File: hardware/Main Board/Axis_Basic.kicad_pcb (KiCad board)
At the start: 4 copper layers, 42 x 42 mm, 78 parts, among them J1 USB4105-GF-A, J2 JST_PH, J3 JST_SH, J4 S2B-PH-K-S, J5 JST_SH, J6 1-84952-4, SW1 RKB2SJK, SW2 RKB2SJK, U1 TLV493D, U2 UA78M33CDCYR, U3 ATSAMD51J19A-AUT, U4 TMC2209-LA, U5 AT25040B-MAHL-T, Y1 32.768

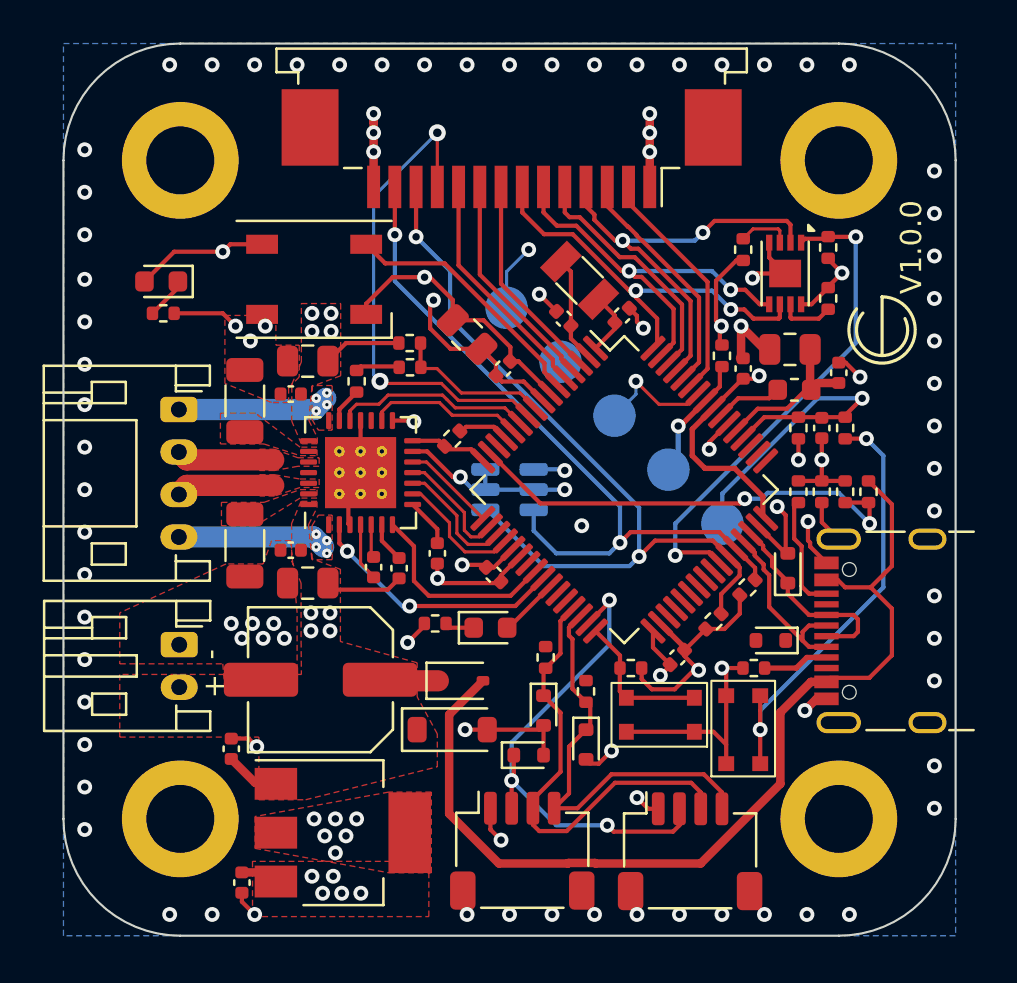
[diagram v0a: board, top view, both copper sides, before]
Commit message: Fix missed connections
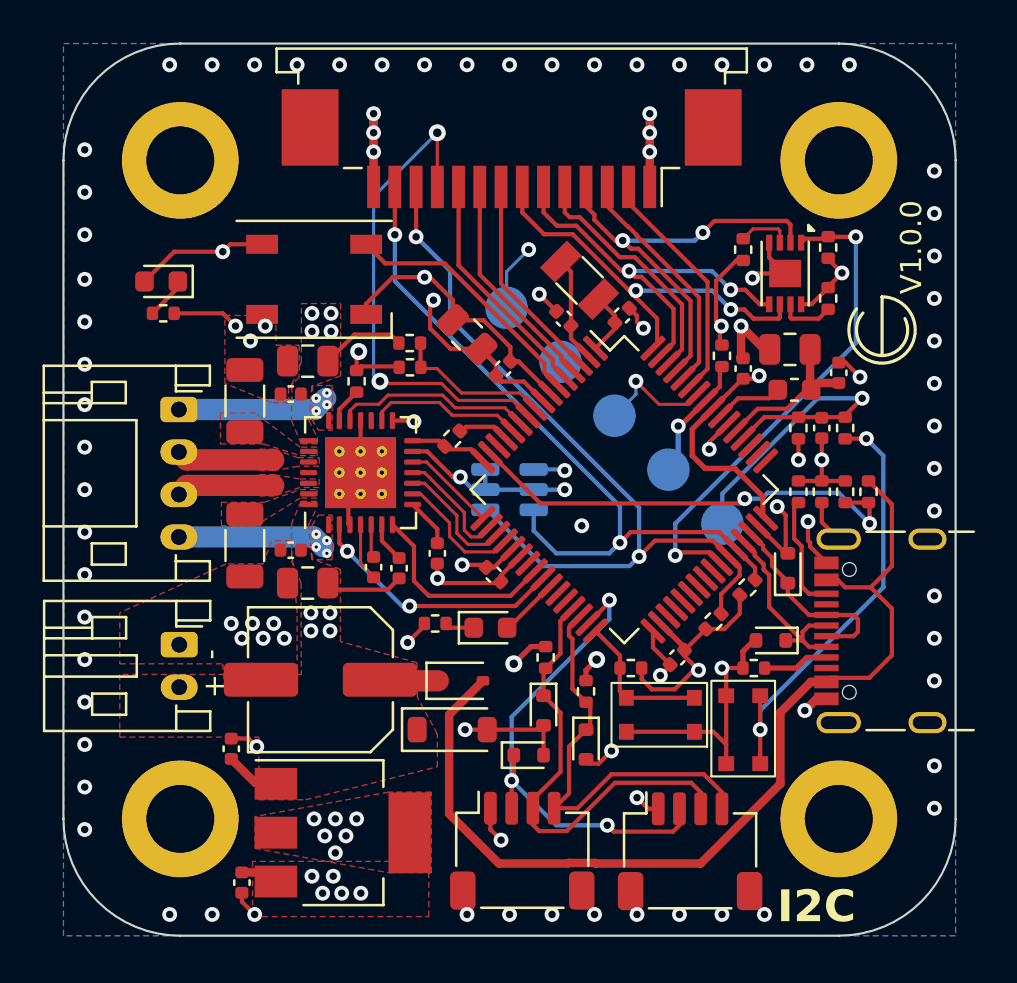
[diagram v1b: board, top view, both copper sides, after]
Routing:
- net +3.3V: track 60.8 -> 63.8 mm, vias 19 -> 21
- net GND: track 92.6 -> 95.1 mm, vias 102 -> 101
- net D-: track 8.70 -> 9.50 mm
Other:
- board text added: "I2C"

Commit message: PCB V1.1.0
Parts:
- removed the D5 at (133.6, 90.2)
- removed the R10 at (133.7, 91.7)
- removed the R11 at (161.0, 88.7)
- removed the R12 at (165.0, 91.0)
- removed the R13 at (165.0, 88.6)
- added C19: 100n, Capacitor_SMD:C_0402_1005Metric, F.Cu at (139.1, 89.3)
- added D6: XZMDK54W-1, LED_SMD:LED_0603_1608Metric, F.Cu at (166.9, 94.4)
- added R18: 1k, Resistor_SMD:R_0402_1005Metric, F.Cu at (166.9, 97.1)
- D1: value NSR0530HT1G -> PMEG3020EJ; footprint Diode_SMD:D_SOD-323 -> Diode_SMD:D_SOD-323F
- U5: value AT25040B-MAHL-T -> 24AA02E-OT; footprint Package_DFN_QFN:DFN-8-1EP_3x2mm_P0.5mm_EP1.3x1.5mm -> Package_TO_SOT_SMD:SOT-23-5
- moved U5 21.2 mm to (141.8, 89.3), turned to 180 degrees
- moved D10 6.01 mm to (134.8, 90.5)
- moved R10 2.19 mm to (159.6, 106.1)
- moved R9 2.19 mm to (161.2, 104.7)
- moved C4 0.22 mm to (137.2, 118.6)
- renumbered 3.3V to 3.3V1, C16 to C10, C19 to C11, C3 to C12, C4 to C13, C5 to C14, C6 to C15, C7 to C16, C8 to C17, C9 to C18, C18 to C2, C10 to C20, C11 to C21, C17 to C3, C2 to C4, C12 to C5, C13 to C6, C14 to C7, C20 to C8, C15 to C9, CLK to CLK1, D7 to D10, D3 to D2, D6 to D3, D8 to D5, D9 to D7, D10 to D8, D2 to D9, GND to GND1, J5 to J4, J4 to J5, R19 to R10, R18 to R11, R17 to R12, R5 to R13, R6 to R14, R7 to R15, R8 to R16, R9 to R17, R16 to R19, R14 to R20, R15 to R21, R22 to R4, R21 to R5, R4 to R6, R23 to R7, R24 to R8, R20 to R9, RST to RST1, DIO to SIO1
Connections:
- net PA03 renamed AUX4
- net PB04 renamed AUX5
- net PB07 renamed AUX6
- net PB30 renamed AUX1
- net PB31 renamed AUX2
- C3 pad 2: PA02 -> Net-(U3-PA01/S1.1)
- J2 pad 1: MOTOR_A1 -> MOTOR_A2
- J2 pad 2: MOTOR_B1 -> MOTOR_A1
- J2 pad 3: MOTOR_A2 -> MOTOR_B1
- J6 pad 8: PA02 -> AUX3
- U3 pad 2: PA02 -> Net-(U3-PA01/S1.1)
- U3 pad 3: PA02 -> AUX3
- U3 pad 42: EEPROM_CS -> unconnected-(U3-PA21/S5.3/S3.3-Pad42)
- U3 pad 43: SCL1 -> SDA1
- U3 pad 44: SDA1 -> SCL1
- U4 pad 21: MOTOR_A1 -> MOTOR_A2
- U4 pad 24: MOTOR_B1 -> MOTOR_A1
- U4 pad 26: MOTOR_A2 -> MOTOR_B1
- U5 pad 1: EEPROM_CS -> SCL1
- U5 pad 2: MISO -> GND
- U5 pad 3: Net-(U5-~{WP}) -> SDA1
- U5 pad 4: GND -> +3.3V
- U5 pad 5: MOSI -> unconnected-(U5-NC-Pad5)
- Y1 pad 2: PA02 -> Net-(U3-PA01/S1.1)
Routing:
- net EEPROM_CS: track 23.6 -> 0.00 mm, vias 2 -> 0
- net PA02: track 14.8 -> 0.00 mm
- net NEOPIX: track 12.0 -> 22.9 mm, vias 0 -> 2
- net AUX3: track 0.00 -> 9.85 mm
- net MISO: track 20.6 -> 11.0 mm, vias 2 -> 0
- net SCK: track 19.3 -> 11.5 mm, vias 2 -> 0
- net MOSI: track 18.9 -> 11.5 mm, vias 2 -> 0
- net RESET: track 16.5 -> 11.0 mm
- net AUX6: track 23.3 -> 17.9 mm
- net Net-(U3-PA01/S1.1): track 0.00 -> 4.96 mm
- net GND: track 95.1 -> 92.1 mm, vias 101 -> 92
- net Net-(U5-~{HOLD}): track 2.60 -> 0.00 mm
- net Net-(U5-~{WP}): track 2.52 -> 0.00 mm
- net MOTOR_A1: track 7.14 -> 4.62 mm, vias 4 -> 0
- net MOTOR_A2: track 4.68 -> 7.14 mm, vias 0 -> 4
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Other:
- board text added: "3.3V"
- board text added: "Aux Port"
- board text added: "CLK"
- board text added: "DIO"
- board text added: "GND"
- board text added: "Motor"
- board text added: "RST"
- board text added: "V1.1.0"
- board text removed: "V1.0.0"

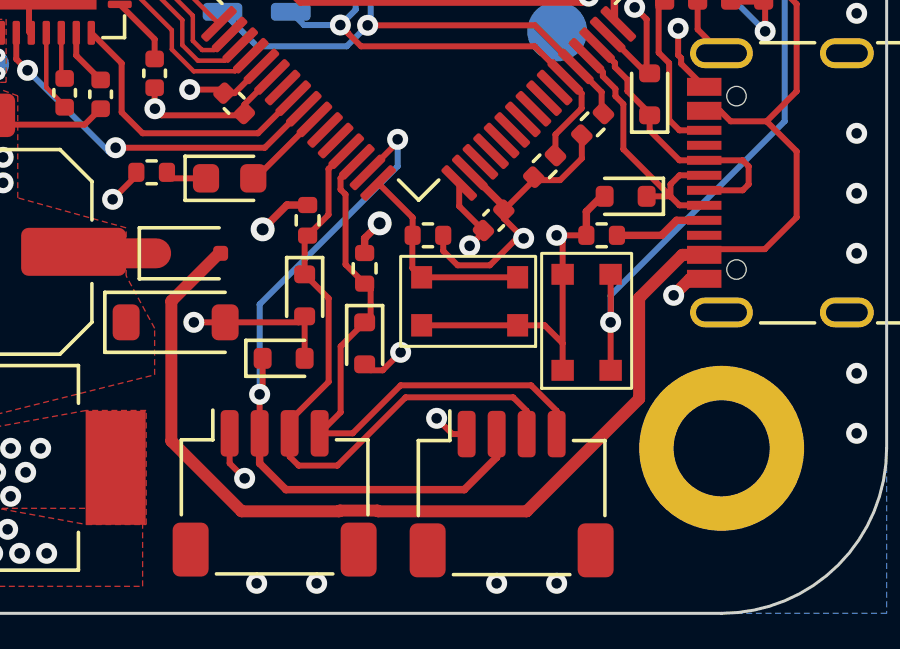
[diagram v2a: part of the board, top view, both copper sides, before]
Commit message: Fix resistor values
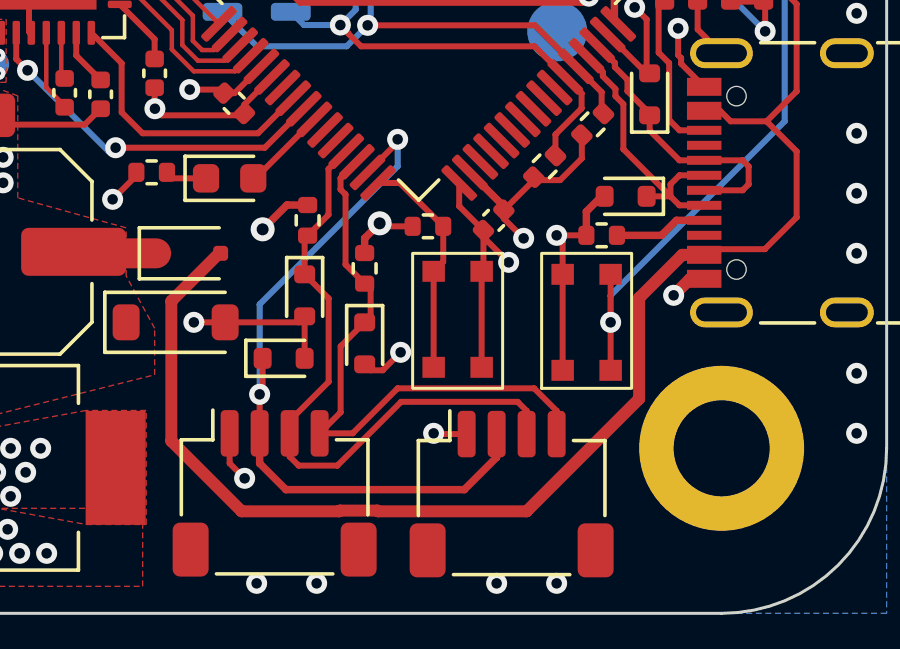
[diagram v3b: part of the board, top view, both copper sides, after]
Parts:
- moved SW2 0.72 mm to (156.7, 111.2), turned to -90 degrees
- moved R17 0.30 mm to (155.7, 108.1), turned to 0 degrees
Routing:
- net +3.3V: track 62.2 -> 59.6 mm
- net User_Input: track 6.95 -> 7.60 mm

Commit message: Update flash part number
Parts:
- C1: value 0.33u -> 1u
- D2: value MMSZ5254B -> MMSZ5254B
- R13: value 300 -> 100
- U5: value 24AA02E-OT -> AT24MAC402
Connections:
- U3 pad 26: USR_LED -> unconnected-(U3-PB13/S4.1-Pad26)
- U3 pad 28: unconnected-(U3-PB15/S4.3-Pad28) -> USR_LED
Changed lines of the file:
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@@
 	(net 64 "AUX4")
 	(net 65 "unconnected-(U3-PA19{slash}S1.3{slash}S3.3-Pad38)")
-	(net 66 "unconnected-(U3-PB15{slash}S4.3-Pad28)")
+	(net 66 "unconnected-(U3-PB13{slash}S4.1-Pad26)")
 	(net 67 "unconnected-(U3-PB17{slash}S5.1-Pad40)")
 	(net 68 "AUX3")
@@
 			)
 		)
-		(property "Value" "0.33u"
+		(property "Value" "1u"
 			(at 0 1.16 90)
 			(layer "F.Fab")
@@
 			)
 		)
-		(property "Value" "24AA02E-OT"
+		(property "Value" "AT24MAC402"
 			(at 0 2.4 0)
 			(layer "F.Fab")
@@
 			)
 		)
-		(property "Value" "300"
+		(property "Value" "100"
 			(at 0 1.17 90)
 			(layer "F.Fab")
@@
 			)
 		)
-		(property "Value" "	MMSZ5254B"
+		(property "Value" "MMSZ5254B"
 			(at 0 2.1 0)
 			(layer "F.Fab")
@@
 			(layers "F.Cu" "F.Paste" "F.Mask")
 			(roundrect_rratio 0.25)
-			(net 56 "USR_LED")
+			(net 66 "unconnected-(U3-PB13{slash}S4.1-Pad26)")
 			(pinfunction "PB13/S4.1")
 			(pintype "bidirectional")
@@
 			(layers "F.Cu" "F.Paste" "F.Mask")
 			(roundrect_rratio 0.25)
-			(net 66 "unconnected-(U3-PB15{slash}S4.3-Pad28)")
+			(net 56 "USR_LED")
 			(pinfunction "PB15/S4.3")
-			(pintype "bidirectional+no_connect")
+			(pintype "bidirectional")
 		)
 		(pad "29" smd roundrect
